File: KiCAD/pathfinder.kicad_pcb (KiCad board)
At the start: 2 copper layers, 64 x 44 mm, 10 parts, among them SW1 SW_Push, SW2 SW_Push, SW3 SW_Push, U1 XIAO-RP2040-DIP

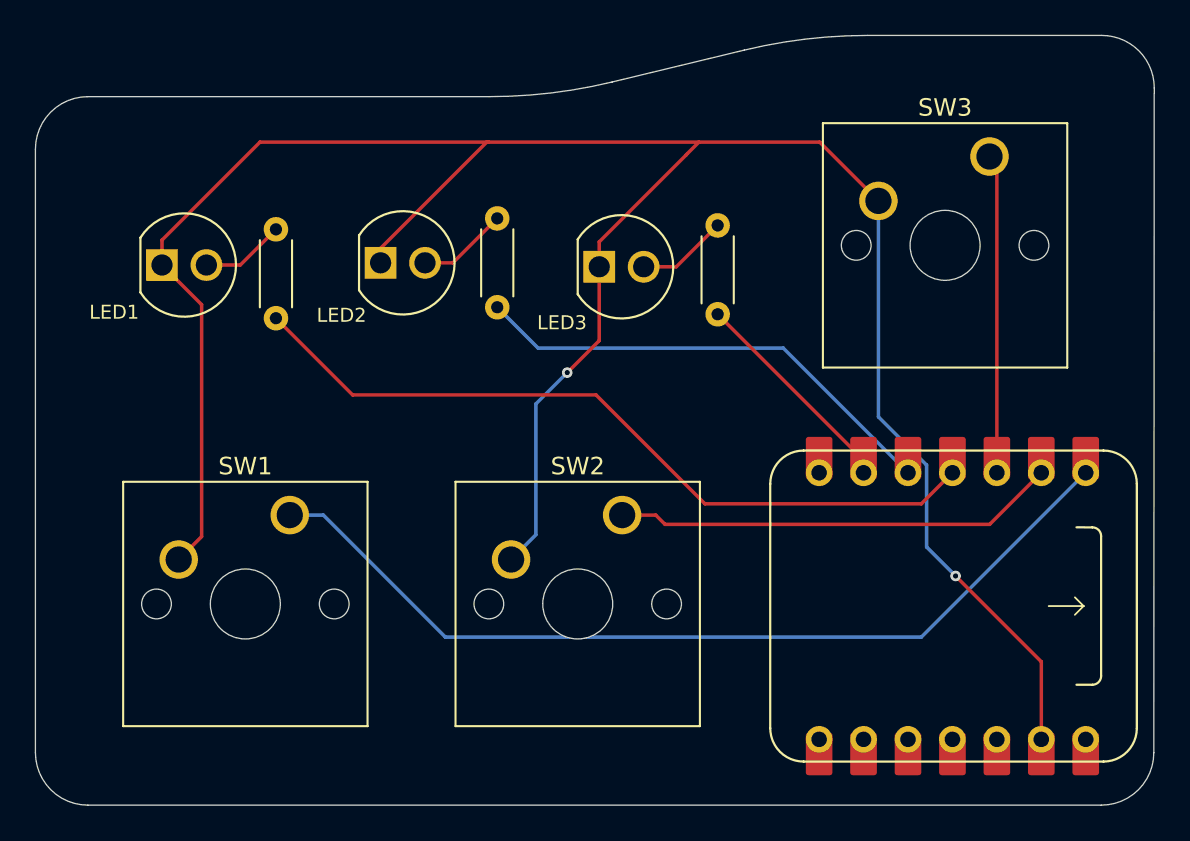
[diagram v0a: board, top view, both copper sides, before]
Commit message: prod folder + how to buy
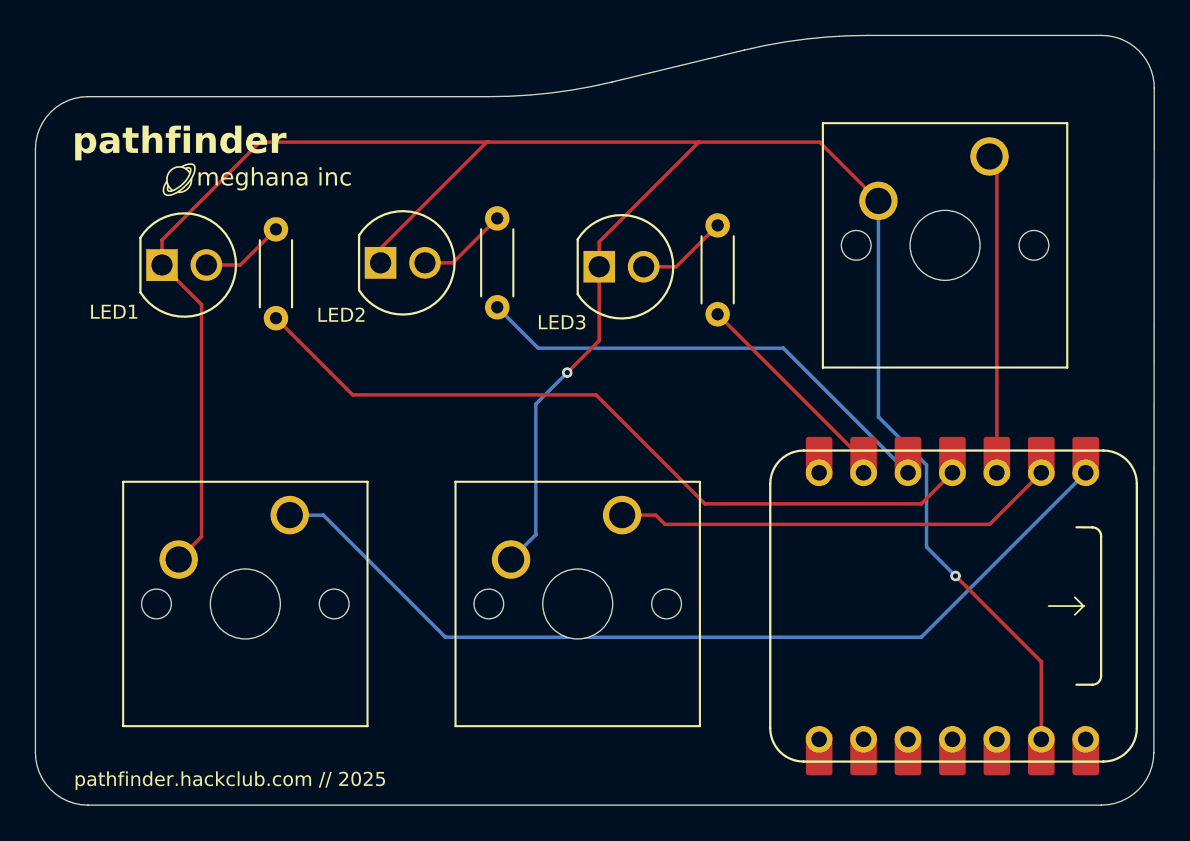
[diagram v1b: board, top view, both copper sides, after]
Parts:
- added G***: LOGO, LOGO, F.Cu at (121.0, 49.5)
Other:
- board text added: "meghana inc"
- board text added: "pathfinder"
- board text added: "pathfinder.hackclub.com // 2025"

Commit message: highlight + extension
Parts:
- added G***: LOGO, LOGO, F.Cu at (116.0, 50.2)

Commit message: change pathfinder background (kicad also updated PCB)
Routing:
- net button1: track 52.3 -> 53.2 mm
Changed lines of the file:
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@@
 			(drillshape 0)
 			(scaleselection 1)
-			(outputdirectory "prod/")
+			(outputdirectory "./")
 		)
 	)
@@
 			(at -3.5 3 0)
 			(layer "F.SilkS")
+			(hide yes)
 			(effects
 				(font
@@
 			(at -3.4 3.2 0)
 			(layer "F.SilkS")
+			(hide yes)
 			(effects
 				(font
@@
 			(at -4.005 2.7 0)
 			(layer "F.SilkS")
+			(hide yes)
 			(effects
 				(font
-					(face "Courier New")
+					(face "Mona Sans")
 					(size 0.8 0.8)
 					(thickness 0.15)
@@
 				(polygon
 					(pts
-						(xy 115.913559 56.563001) (xy 115.913559 57.110105) (xy 116.218521 57.110105) (xy 116.218521 56.928779)
-						(xy 116.220404 56.913546) (xy 116.225066 56.904794) (xy 116.232543 56.899361) (xy 116.242017 56.897516)
-						(xy 116.251044 56.899274) (xy 116.258381 56.904501) (xy 116.263055 56.913116) (xy 116.264976 56.928779)
-						(xy 116.264976 57.157) (xy 115.75783 57.157) (xy 115.742929 57.155086) (xy 115.734285 57.150307)
-						(xy 115.728987 57.142807) (xy 115.727202 57.133552) (xy 115.729021 57.123886) (xy 115.734285 57.116553)
-						(xy 115.742903 57.111957) (xy 115.75783 57.110105) (xy 115.867104 57.110105) (xy 115.867104 56.563001)
-						(xy 115.75783 56.563001) (xy 115.742898 56.561161) (xy 115.734285 56.556602) (xy 115.72902 56.549228)
-						(xy 115.727202 56.539554) (xy 115.729021 56.529887) (xy 115.734285 56.522554) (xy 115.742903 56.517958)
-						(xy 115.75783 56.516106) (xy 116.022833 56.516106) (xy 116.037752 56.51796) (xy 116.046329 56.522554)
-						(xy 116.051631 56.529892) (xy 116.053461 56.539554) (xy 116.051633 56.549224) (xy 116.046329 56.556602)
-						(xy 116.037757 56.56116) (xy 116.022833 56.563001)
+						(xy 115.823336 57.157) (xy 116.332924 57.157) (xy 116.332924 57.086462) (xy 115.899491 57.086462)
+						(xy 115.899491 56.341033) (xy 115.823336 56.341033)
 					)
 				)
 				(polygon
 					(pts
-						(xy 116.514983 56.847495) (xy 116.514983 57.110105) (xy 116.868011 57.110105) (xy 116.868011 56.975674)
-						(xy 116.869819 56.960409) (xy 116.874264 56.951689) (xy 116.881506 56.946267) (xy 116.89097 56.944411)
-						(xy 116.900425 56.946269) (xy 116.907627 56.951689) (xy 116.912108 56.960414) (xy 116.913929 56.975674)
-						(xy 116.913929 57.157) (xy 116.40732 57.157) (xy 116.392463 57.155087) (xy 116.383824 57.150307)
-						(xy 116.378527 57.142807) (xy 116.376741 57.133552) (xy 116.378561 57.123886) (xy 116.383824 57.116553)
-						(xy 116.392437 57.111955) (xy 116.40732 57.110105) (xy 116.469065 57.110105) (xy 116.469065 56.563001)
-						(xy 116.40732 56.563001) (xy 116.392432 56.561163) (xy 116.383824 56.556602) (xy 116.378559 56.549228)
-						(xy 116.376741 56.539554) (xy 116.378561 56.529887) (xy 116.383824 56.522554) (xy 116.392437 56.517957)
-						(xy 116.40732 56.516106) (xy 116.889895 56.516106) (xy 116.889895 56.672422) (xy 116.888077 56.687689)
-						(xy 116.883594 56.696455) (xy 116.876396 56.701837) (xy 116.866936 56.703685) (xy 116.857468 56.701839)
-						(xy 116.85023 56.696455) (xy 116.845784 56.687694) (xy 116.843978 56.672422) (xy 116.843978 56.563001)
-						(xy 116.514983 56.563001) (xy 116.514983 56.8006) (xy 116.679456 56.8006) (xy 116.679456 56.750579)
-						(xy 116.681339 56.735346) (xy 116.686001 56.726595) (xy 116.693478 56.721161) (xy 116.702952 56.719316)
-						(xy 116.711955 56.721137) (xy 116.719316 56.726595) (xy 116.724015 56.735351) (xy 116.725911 56.750579)
-						(xy 116.725911 56.897516) (xy 116.724017 56.912752) (xy 116.719316 56.921549) (xy 116.711959 56.926968)
-						(xy 116.702952 56.928779) (xy 116.693474 56.926945) (xy 116.686001 56.921549) (xy 116.681337 56.912757)
-						(xy 116.679456 56.897516) (xy 116.679456 56.847495)
+						(xy 116.447816 57.157) (xy 116.998828 57.157) (xy 116.998828 57.087586) (xy 116.523971 57.087586)
+						(xy 116.523971 56.77178) (xy 116.946169 56.77178) (xy 116.946169 56.706811) (xy 116.523971 56.706811)
+						(xy 116.523971 56.409372) (xy 116.998828 56.409372) (xy 116.998828 56.341033) (xy 116.447816 56.341033)
 					)
 				)
 				(polygon
 					(pts
-						(xy 117.402008 56.518868) (xy 117.437075 56.526949) (xy 117.469679 56.540237) (xy 117.513244 56.567035)
-						(xy 117.542659 56.594997) (xy 117.58098 56.649088) (xy 117.608262 56.705101) (xy 117.619879 56.749537)
-						(xy 117.624089 56.804801) (xy 117.624089 56.868304) (xy 117.620655 56.914751) (xy 117.610342 56.960256)
-						(xy 117.592924 57.005276) (xy 117.56839 57.046455) (xy 117.534255 57.084887) (xy 117.489121 57.120852)
-						(xy 117.451612 57.140751) (xy 117.410214 57.15284) (xy 117.363971 57.157) (xy 117.116943 57.157)
-						(xy 117.102086 57.155087) (xy 117.093447 57.150307) (xy 117.08815 57.142807) (xy 117.086364 57.133552)
-						(xy 117.088184 57.123886) (xy 117.093447 57.116553) (xy 117.10206 57.111955) (xy 117.116943 57.110105)
-						(xy 117.155729 57.110105) (xy 117.201647 57.110105) (xy 117.368318 57.110105) (xy 117.405737 57.106007)
-						(xy 117.441652 57.093665) (xy 117.476811 57.072443) (xy 117.508129 57.045227) (xy 117.533274 57.015189)
-						(xy 117.55277 56.982073) (xy 117.572027 56.928871) (xy 117.578172 56.878074) (xy 117.578172 56.79508)
-						(xy 117.574607 56.754009) (xy 117.564494 56.71917) (xy 117.541005 56.672235) (xy 117.508758 56.626895)
-						(xy 117.485663 56.60483) (xy 117.450823 56.582931) (xy 117.411203 56.568015) (xy 117.368318 56.563001)
-						(xy 117.201647 56.563001) (xy 117.201647 57.110105) (xy 117.155729 57.110105) (xy 117.155729 56.563001)
-						(xy 117.116943 56.563001) (xy 117.102055 56.561163) (xy 117.093447 56.556602) (xy 117.088182 56.549228)
-						(xy 117.086364 56.539554) (xy 117.088184 56.529887) (xy 117.093447 56.522554) (xy 117.10206 56.517957)
-						(xy 117.116943 56.516106) (xy 117.363971 56.516106)
+						(xy 117.497007 56.343851) (xy 117.563701 56.357545) (xy 117.594141 56.368418) (xy 117.622731 56.381897)
+						(xy 117.649522 56.397972) (xy 117.67436 56.416525) (xy 117.697503 56.437792) (xy 117.718547 56.461455)
+						(xy 117.737843 56.488044) (xy 117.754846 56.516977) (xy 117.769876 56.549059) (xy 117.78238 56.583441)
+						(xy 117.79255 56.621113) (xy 117.799931 56.661029) (xy 117.804547 56.704236) (xy 117.806099 56.749602)
+						(xy 117.802611 56.816624) (xy 117.788325 56.894711) (xy 117.764211 56.962362) (xy 117.731325 57.019822)
+						(xy 117.690356 57.0674) (xy 117.641583 57.105268) (xy 117.614202 57.120557) (xy 117.584925 57.133277)
+						(xy 117.553421 57.143457) (xy 117.520068 57.150855) (xy 117.484255 57.15545) (xy 117.446623 57.157)
+						(xy 117.136385 57.157) (xy 117.136385 57.087586) (xy 117.211417 57.087586) (xy 117.438758 57.087586)
+						(xy 117.49349 57.083371) (xy 117.550619 57.068175) (xy 117.576325 57.056649) (xy 117.60018 57.042567)
+						(xy 117.622335 57.025827) (xy 117.642514 57.00661) (xy 117.661068 56.984448) (xy 117.677455 56.959826)
+						(xy 117.692055 56.931878) (xy 117.704234 56.901452) (xy 117.714247 56.867358) (xy 117.721535 56.830764)
+						(xy 117.726145 56.79031) (xy 117.727697 56.747355) (xy 117.722998 56.674121) (xy 117.707769 56.604465)
+						(xy 117.683362 56.546265) (xy 117.650716 56.498656) (xy 117.631428 56.478593) (xy 117.610208 56.460999)
+						(xy 117.586873 56.445771) (xy 117.561699 56.433141) (xy 117.534103 56.422949) (xy 117.504723 56.415562)
+						(xy 117.472613 56.410927) (xy 117.438758 56.409372) (xy 117.211417 56.409372) (xy 117.211417 57.087586)
+						(xy 117.136385 57.087586) (xy 117.136385 56.341033) (xy 117.446623 56.341033)
 					)
 				)
 				(polygon
 					(pts
-						(xy 118.029874 56.462959) (xy 118.029874 57.110105) (xy 118.187264 57.110105) (xy 118.202183 57.111959)
-						(xy 118.210761 57.116553) (xy 118.216062 57.12389) (xy 118.217893 57.133552) (xy 118.216096 57.142803)
-						(xy 118.210761 57.150307) (xy 118.202157 57.155084) (xy 118.187264 57.157) (xy 117.826567 57.157)
-						(xy 117.811709 57.155087) (xy 117.80307 57.150307) (xy 117.797773 57.142807) (xy 117.795987 57.133552)
-						(xy 117.797807 57.123886) (xy 117.80307 57.116553) (xy 117.811683 57.111955) (xy 117.826567 57.110105)
-						(xy 117.983957 57.110105) (xy 117.983957 56.525485) (xy 117.834236 56.572233) (xy 117.81836 56.575506)
-						(xy 117.810691 56.573891) (xy 117.803364 56.568765) (xy 117.798213 56.561327) (xy 117.796525 56.552792)
-						(xy 117.801996 56.537648) (xy 117.820021 56.528416)
+						(xy 118.081556 57.157) (xy 118.156588 57.157) (xy 118.156588 56.337907) (xy 118.08268 56.337907)
+						(xy 118.078783 56.365362) (xy 118.071727 56.390044) (xy 118.062947 56.408912) (xy 118.051504 56.425453)
+						(xy 118.038568 56.438446) (xy 118.023159 56.449288) (xy 117.985281 56.463943) (xy 117.934815 56.469212)
+						(xy 117.890021 56.469212) (xy 117.890021 56.526071) (xy 118.081556 56.526071)
 					)
 				)
@@
 	)
 	(segment
-		(start 127.04 68.42)
+		(start 137.04 76.5)
 		(end 128.96 68.42)
 		(width 0.2)
@@
 	(segment
 		(start 172.54 66)
-		(end 163.14 75.4)
+		(end 162.04 76.5)
 		(width 0.2)
 		(layer "B.Cu")
@@
 	(segment
 		(start 128.96 68.42)
-		(end 135.94 75.4)
+		(end 127.04 68.42)
 		(width 0.2)
 		(layer "B.Cu")
@@
 	)
 	(segment
-		(start 163.14 75.4)
-		(end 135.94 75.4)
+		(start 162.04 76.5)
+		(end 137.04 76.5)
 		(width 0.2)
 		(layer "B.Cu")
